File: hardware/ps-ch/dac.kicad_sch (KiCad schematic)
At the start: 5 parts, among them U4 AD5693RBCPZ

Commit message: did some wiring
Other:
- note added: "DAC"
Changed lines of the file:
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@@
+		)
+	)
+	(text "DAC"
+		(exclude_from_sim no)
+		(at 147.32 40.64 0)
+		(effects
+			(font
+				(size 6.35 6.35)
+				(thickness 1.27)
+				(bold yes)
+			)
 		)
 	)

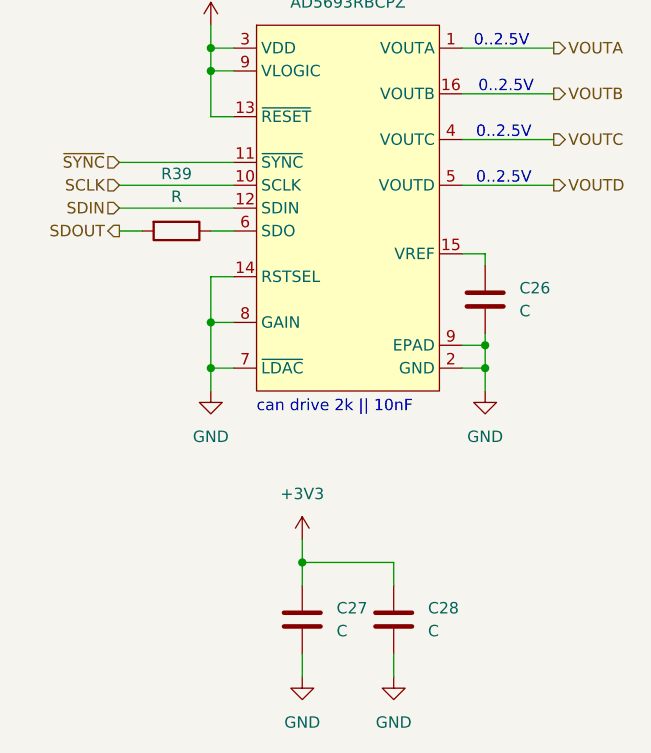
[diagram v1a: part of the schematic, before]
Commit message: - added component values/part numbers
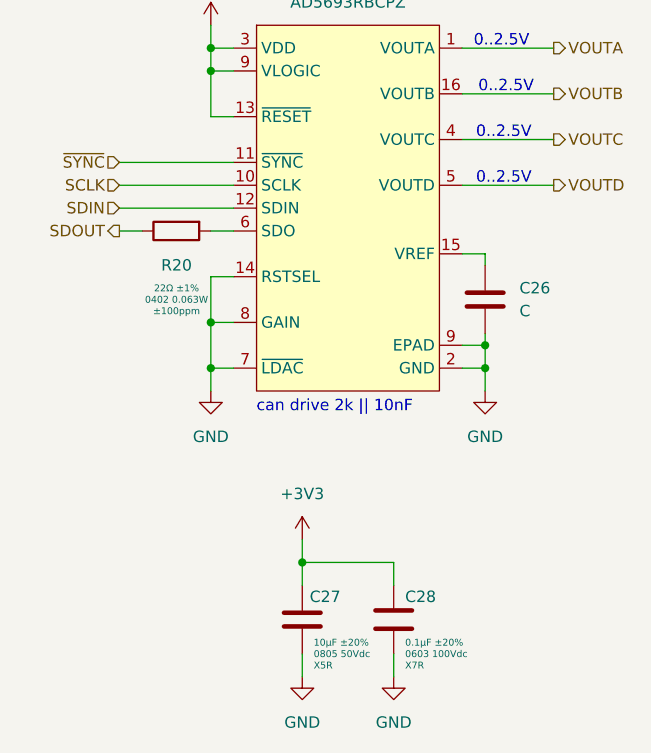
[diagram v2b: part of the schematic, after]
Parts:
- removed C27, C28: C, symbol Device:C
- removed R39: R, symbol Device:R
- added C27: 10μF 0805 50Vdc X5R ±20%, Capacitor_SMD:C_0805_2012Metric, symbol ps-ch:10μF 0805 50Vdc X5R ±20%
- added C28: 0.1μF 0603 100Vdc X7R ±20%, Capacitor_SMD:C_0603_1608Metric, symbol ps-ch:0.1μF 0603 100Vdc X7R ±20%
- added R20: 22Ω 0402 0.063W ±1% ±100ppm/°C, Resistor_SMD:R_0402_1005Metric, symbol ps-ch:22Ω 0402 0.063W ±1% ±100ppm/°C
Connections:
- net +3V3: now also C27.2, C28.2
- net GND: now also C27.1, C28.1
- net SDOUT: now also R20.1
- net at U4.6 (SDO): now also R20.2

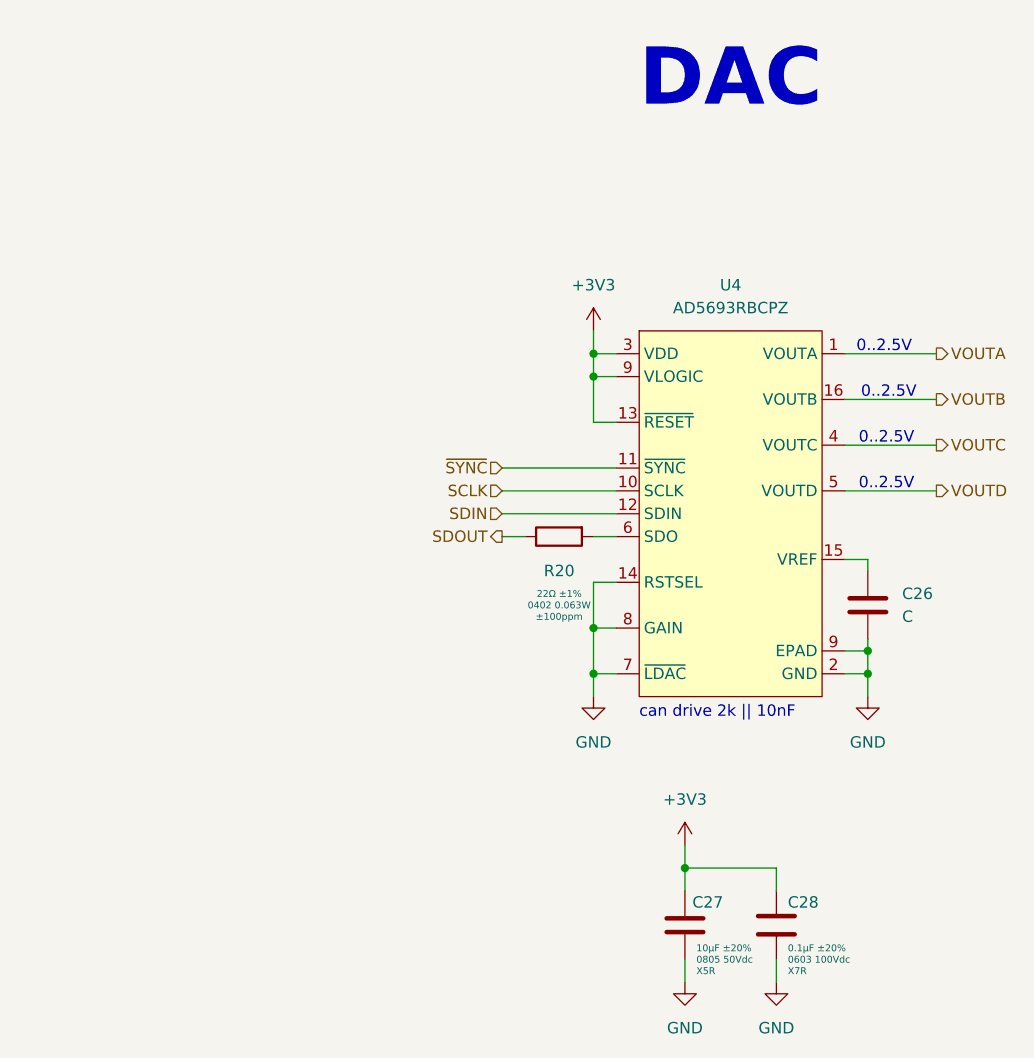
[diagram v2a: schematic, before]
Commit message: calculated voltage correction
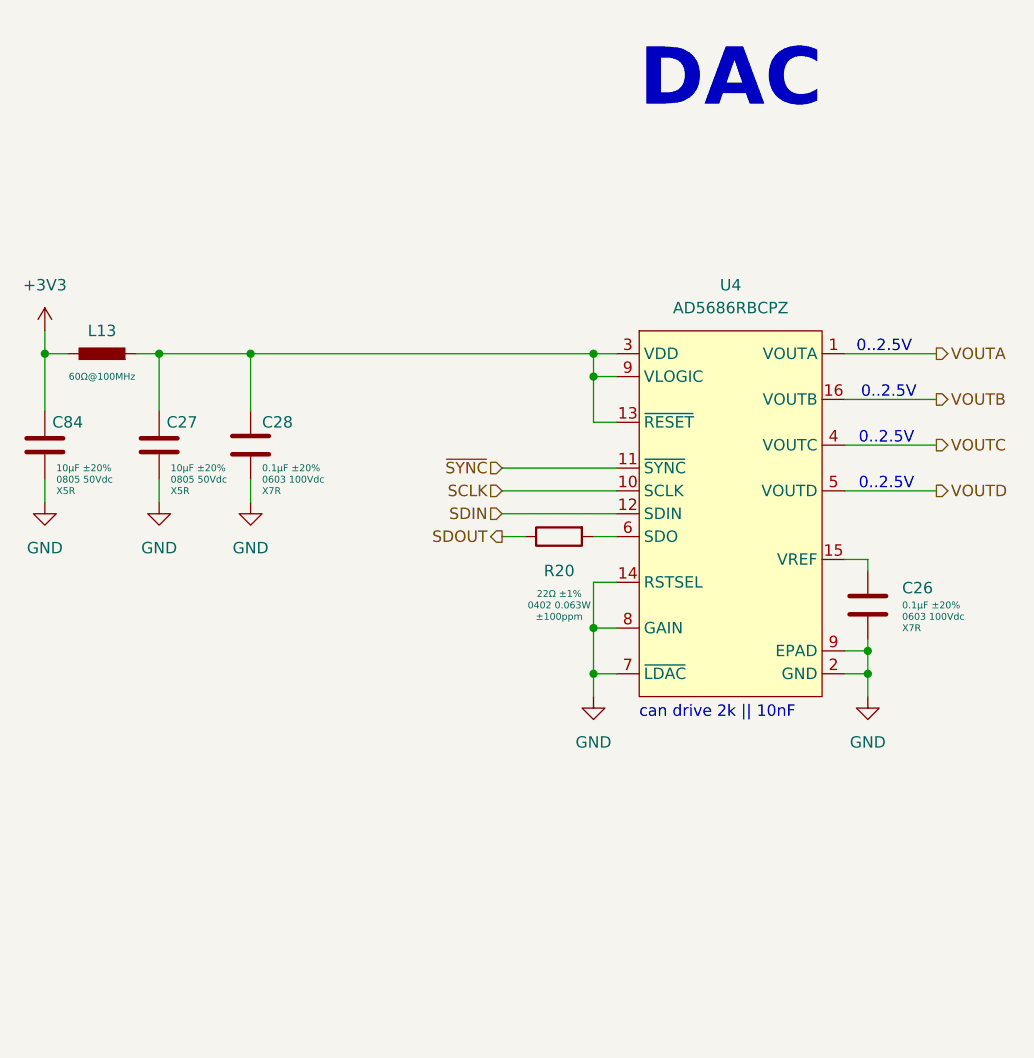
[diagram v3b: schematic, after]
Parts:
- removed C26: C, symbol Device:C
- added C26: 0.1μF 0603 100Vdc X7R ±20%, Capacitor_SMD:C_0603_1608Metric, symbol ps-ch:0.1μF 0603 100Vdc X7R ±20%
- added C84: 10μF 0805 50Vdc X5R ±20%, Capacitor_SMD:C_0805_2012Metric, symbol ps-ch:10μF 0805 50Vdc X5R ±20%
- added L13: 60Ω@100MHz, Inductor_SMD:L_0603_1608Metric, symbol ps-ch:74437349015
- U4: value AD5693RBCPZ -> AD5686RBCPZ
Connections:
- net +3V3: now also C84.2, L13.2; no longer C27.2, C28.2, U4.13 (~{RESET}), U4.3 (VDD), U4.9 (EPAD)
- net GND: now also C26.1, C84.1
- net at U4.15 (VREF): now also C26.2
- new net: C27.2, C28.2, L13.1, U4.13 (~{RESET}), U4.3 (VDD), U4.9 (EPAD)
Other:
- moved on the sheet: C27, C28

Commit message: assigned footprints
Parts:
- U4: value AD5686RBCPZ -> AD5686RBRUZ; footprint (none) -> Package_SO:TSSOP-16_4.4x5mm_P0.65mm; symbol ps-ch:AD5686RBCPZ -> ps-ch:AD5686RBRUZ; Manufacturer (none) -> Analog Devices; Manufacturer Part Number (none) -> AD5686RBRUZ-RL7
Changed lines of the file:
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@@
 	)
 	(symbol
-		(lib_id "ps-ch:AD5686RBCPZ")
+		(lib_id "ps-ch:AD5686RBRUZ")
 		(at 147.32 88.9 0)
 		(unit 1)
@@
 			)
 		)
-		(property "Value" "AD5686RBCPZ"
+		(property "Value" "AD5686RBRUZ"
 			(at 147.32 66.04 0)
 			(effects
@@
 			)
 		)
-		(property "Footprint" ""
-			(at 180.34 97.79 0)
+		(property "Footprint" "Package_SO:TSSOP-16_4.4x5mm_P0.65mm"
+			(at 147.32 60.96 0)
 			(effects
 				(font
@@
 			(effects
 				(font
+					(size 1.27 1.27)
+				)
+				(hide yes)
+			)
+		)
+		(property "Manufacturer" "Analog Devices"
+			(at 147.32 55.88 0)
+			(effects
+				(font
+					(size 1.27 1.27)
+				)
+				(hide yes)
+			)
+		)
+		(property "Manufacturer Part Number" "AD5686RBRUZ-RL7"
+			(at 147.32 58.42 0)
+			(effects
+				(font

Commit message: first pcb sync
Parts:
- renumbered C84 to C61, C27 to C62, C28 to C63, C26 to C64, L13 to L10, R20 to R49, U4 to U11
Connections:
- net GND: now also U11.10 (GAIN), U11.16 (RSTSEL), U11.4 (GND); no longer U11.14 (RSTSEL), U11.2 (GND), U11.7 (~{LDAC}), U11.8 (GAIN)
- net SCLK: now also U11.12 (SCLK); no longer U11.10 (SCLK)
- net SDIN: now also U11.14 (SDIN); no longer U11.12 (SDIN)
- net VOUTA: now also U11.3 (VOUTA); no longer U11.1 (VOUTA)
- net VOUTB: now also U11.2 (VOUTB); no longer U11.16 (VOUTB)
- net VOUTC: now also U11.6 (VOUTC); no longer U11.4 (VOUTC)
- net VOUTD: now also U11.7 (VOUTD); no longer U11.5 (VOUTD)
- net ~{SYNC}: now also U11.13 (~{SYNC}); no longer U11.11 (~{SYNC})
- net at C62.2, C63.2, L10.1: now also U11.11 (VLOGIC), U11.15 (~{RESET}), U11.5 (VDD); no longer U11.13 (~{RESET}), U11.3 (VDD), U11.9 (EPAD)
- net at C64.2: now also U11.1 (VREF); no longer U11.15 (VREF)
- net at R49.2: now also U11.8 (SDO); no longer U11.6 (SDO)
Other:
- moved on the sheet: C64
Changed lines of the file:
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@@
-	)
-	(junction
-		(at 162.56 104.14)
-		(diameter 0)
-		(color 0 0 0 0)
 	)
 	(junction
@@
 	(wire
 		(pts
-			(xy 162.56 93.98) (xy 162.56 95.25)
+			(xy 162.56 93.98) (xy 162.56 96.52)
 		)
 		(stroke
@@
 	(wire
 		(pts
-			(xy 160.02 104.14) (xy 162.56 104.14)
-		)
-		(stroke
-			(width 0)
-			(type default)
-		)
-	)
-	(wire
-		(pts
 			(xy 73.66 71.12) (xy 71.12 71.12)
-		)
-		(stroke
-			(width 0)
-			(type default)
-		)
-	)
-	(wire
-		(pts
-			(xy 162.56 102.87) (xy 162.56 104.14)
 		)
 		(stroke
@@
 		(dnp no)
 		(fields_autoplaced yes)
-		(property "Reference" "U4"
+		(property "Reference" "U11"
 			(at 147.32 63.5 0)
 			(effects
@@
 		)
 		(pin "12"
-		)
-		(pin "9"
 		)
 		(pin "16"
@@
 			(project "ps-ch"
 				(path "/431acd2e-2ab9-4aa9-b759-273f044decc5/102c0564-cdac-4adc-aea7-12628d924237"
-					(reference "U4")
+					(reference "U11")
 					(unit 1)
 				)
@@
 		(dnp no)
 		(fields_autoplaced yes)
-		(property "Reference" "#PWR037"
+		(property "Reference" "#PWR0117"
 			(at 93.98 93.98 0)
 			(effects
@@
 			(project "ps-ch"
 				(path "/431acd2e-2ab9-4aa9-b759-273f044decc5/102c0564-cdac-4adc-aea7-12628d924237"
-					(reference "#PWR037")
+					(reference "#PWR0117")
 					(unit 1)
 				)
@@
 		(dnp no)
 		(fields_autoplaced yes)
-		(property "Reference" "#PWR033"
+		(property "Reference" "#PWR0119"
 			(at 162.56 115.57 0)
 			(effects
@@
 			(project "ps-ch"
 				(path "/431acd2e-2ab9-4aa9-b759-273f044decc5/102c0564-cdac-4adc-aea7-12628d924237"
-					(reference "#PWR033")
+					(reference "#PWR0119")
 					(unit 1)
 				)
@@
 		(dnp no)
 		(fields_autoplaced yes)
-		(property "Reference" "#PWR0149"
+		(property "Reference" "#PWR0114"
 			(at 71.12 72.39 0)
 			(effects
@@
 			(project "ps-ch"
 				(path "/431acd2e-2ab9-4aa9-b759-273f044decc5/102c0564-cdac-4adc-aea7-12628d924237"
-					(reference "#PWR0149")
+					(reference "#PWR0114")
 					(unit 1)
 				)
@@
 		(on_board yes)
 		(dnp no)
-		(property "Reference" "C27"
+		(property "Reference" "C62"
 			(at 86.36 78.74 0)
 			(effects
@@
 			(project "ps-ch"
 				(path "/431acd2e-2ab9-4aa9-b759-273f044decc5/102c0564-cdac-4adc-aea7-12628d924237"
-					(reference "C27")
+					(reference "C62")
 					(unit 1)
 				)
@@
 		(dnp no)
 		(fields_autoplaced yes)
-		(property "Reference" "#PWR036"
+		(property "Reference" "#PWR0116"
 			(at 83.82 93.98 0)
 			(effects
@@
 			(project "ps-ch"
 				(path "/431acd2e-2ab9-4aa9-b759-273f044decc5/102c0564-cdac-4adc-aea7-12628d924237"
-					(reference "#PWR036")
+					(reference "#PWR0116")
 					(unit 1)
 				)
@@
 		(on_board yes)
 		(dnp no)
-		(property "Reference" "C28"
+		(property "Reference" "C63"
 			(at 95.25 78.74 0)
 			(effects
@@
 			(project "ps-ch"
 				(path "/431acd2e-2ab9-4aa9-b759-273f044decc5/102c0564-cdac-4adc-aea7-12628d924237"
-					(reference "C28")
+					(reference "C63")
 					(unit 1)
 				)
@@
 	(symbol
 		(lib_id "ps-ch:0.1μF 0603 100Vdc X7R ±20%")
-		(at 162.56 99.06 0)
+		(at 162.56 100.33 0)
 		(unit 1)
 		(exclude_from_sim no)
@@
 		(dnp no)
 		(fields_autoplaced yes)
-		(property "Reference" "C26"
-			(at 166.37 97.1549 0)
+		(property "Reference" "C64"
+			(at 166.37 98.4249 0)
 			(effects
 				(font
@@
 		)
 		(property "Value" "0.1μF 0603 100Vdc X7R ±20%"
-			(at 162.56 83.82 0)
+			(at 162.56 85.09 0)
 			(effects
 				(font
@@
 		)
 		(property "Footprint" "Capacitor_SMD:C_0603_1608Metric"
-			(at 162.56 88.9 0)
+			(at 162.56 90.17 0)
 			(effects
 				(font
@@
 		)
 		(property "Datasheet" "~"
-			(at 162.56 99.06 90)
+			(at 162.56 100.33 90)
 			(effects
 				(font
@@
 		)
 		(property "Description" "Capacitor 0603 100Vdc X7R ±20%"
-			(at 162.56 86.36 0)
+			(at 162.56 87.63 0)
 			(effects
 				(font
@@
 		)
 		(property "Manufacturer" "Murata"
-			(at 162.56 78.74 0)
+			(at 162.56 80.01 0)
 			(effects
 				(font
@@
 		)
 		(property "Manufacturer Part Number" "GRM188R72A104MA35"
-			(at 162.56 81.28 0)
+			(at 162.56 82.55 0)
 			(effects
 				(font
@@
 		)
 		(property "DisplayValue0" "0.1μF ±20%"
-			(at 166.37 99.06 0)
+			(at 166.37 100.33 0)
 			(effects
 				(font
@@
 		)
 		(property "DisplayValue1" "0603 100Vdc"
-			(at 166.37 100.33 0)
+			(at 166.37 101.6 0)
 			(effects
 				(font
@@
 		)
 		(property "DisplayValue2" "X7R"
-			(at 166.37 101.6 0)
+			(at 166.37 102.87 0)
 			(effects
 				(font
@@
 			(project "ps-ch"
 				(path "/431acd2e-2ab9-4aa9-b759-273f044decc5/102c0564-cdac-4adc-aea7-12628d924237"
-					(reference "C26")
+					(reference "C64")
 					(unit 1)
 				)
@@
 		(on_board yes)
 		(dnp no)
-		(property "Reference" "L13"
+		(property "Reference" "L10"
 			(at 77.47 68.58 90)
 			(effects
@@
 			(project "ps-ch"
 				(path "/431acd2e-2ab9-4aa9-b759-273f044decc5/102c0564-cdac-4adc-aea7-12628d924237"
-					(reference "L13")
+					(reference "L10")
 					(unit 1)
 				)
@@
 		(on_board yes)
 		(dnp no)
-		(property "Reference" "R20"
+		(property "Reference" "R49"
 			(at 128.27 95.25 90)
 			(effects
@@
 			(project "ps-ch"
 				(path "/431acd2e-2ab9-4aa9-b759-273f044decc5/102c0564-cdac-4adc-aea7-12628d924237"
-					(reference "R20")
+					(reference "R49")
 					(unit 1)
 				)
@@
 		(dnp no)
 		(fields_autoplaced yes)
-		(property "Reference" "#PWR0150"
+		(property "Reference" "#PWR0115"
 			(at 71.12 93.98 0)
 			(effects
@@
 			(project "ps-ch"
 				(path "/431acd2e-2ab9-4aa9-b759-273f044decc5/102c0564-cdac-4adc-aea7-12628d924237"
-					(reference "#PWR0150")
+					(reference "#PWR0115")
 					(unit 1)
 				)
@@
 		(on_board yes)
 		(dnp no)
-		(property "Reference" "C84"
+		(property "Reference" "C61"
 			(at 73.66 78.74 0)
 			(effects
@@
 			(project "ps-ch"
 				(path "/431acd2e-2ab9-4aa9-b759-273f044decc5/102c0564-cdac-4adc-aea7-12628d924237"
-					(reference "C84")
+					(reference "C61")
 					(unit 1)
 				)
@@
 		(dnp no)
 		(fields_autoplaced yes)
-		(property "Reference" "#PWR038"
+		(property "Reference" "#PWR0118"
 			(at 132.08 115.57 0)
 			(effects
@@
 			(project "ps-ch"
 				(path "/431acd2e-2ab9-4aa9-b759-273f044decc5/102c0564-cdac-4adc-aea7-12628d924237"
-					(reference "#PWR038")
+					(reference "#PWR0118")
 					(unit 1)
 				)
